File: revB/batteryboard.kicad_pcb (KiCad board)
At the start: 2 copper layers, 90.2 x 101.1 mm, 50 parts, among them J101 KEYSTONE-1042, J102 KEYSTONE-1042, J103 KEYSTONE-1042, J104 KEYSTONE-1042, J105 KEYSTONE-1042, J106 KEYSTONE-1042, J107 Conn_02x10_Top_Bottom, P201 Conn_02x60_Top_Bottom, Q101 IRF7458, Q102 IRF7458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

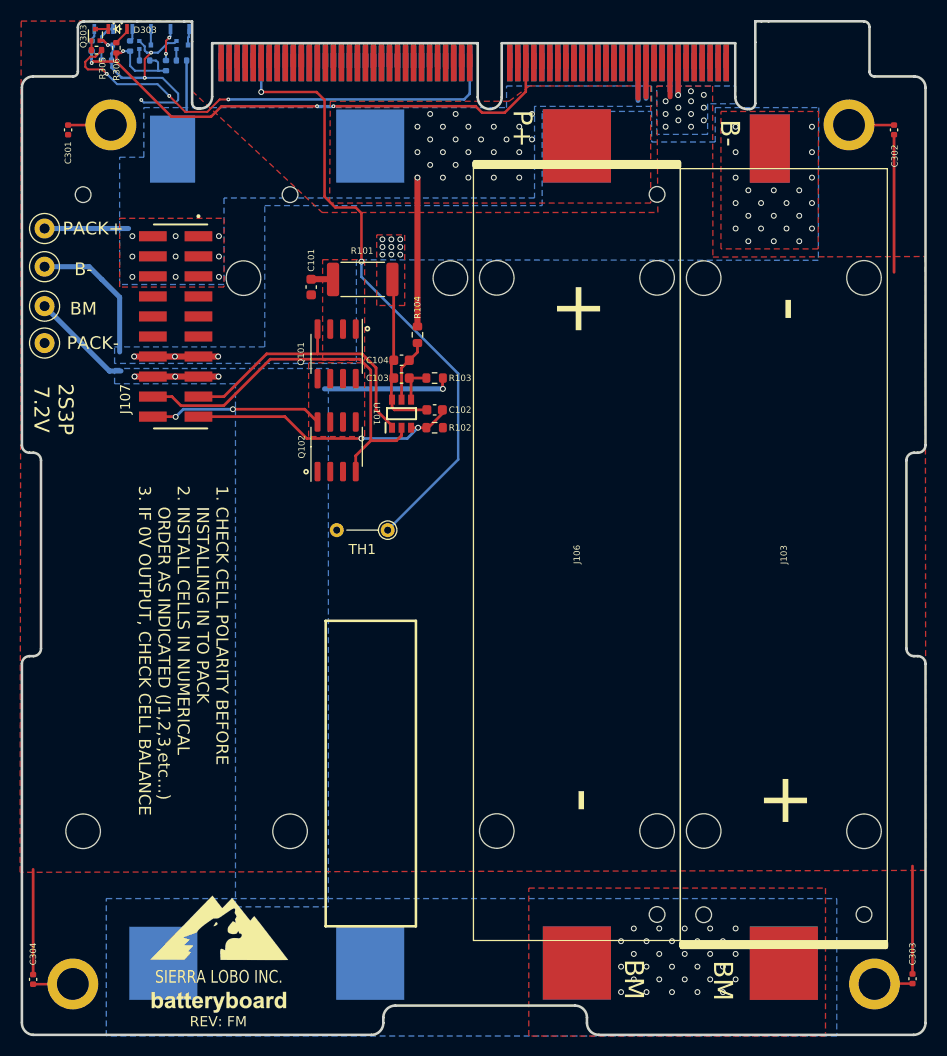
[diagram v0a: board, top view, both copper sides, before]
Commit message: update project to kicad 7 format
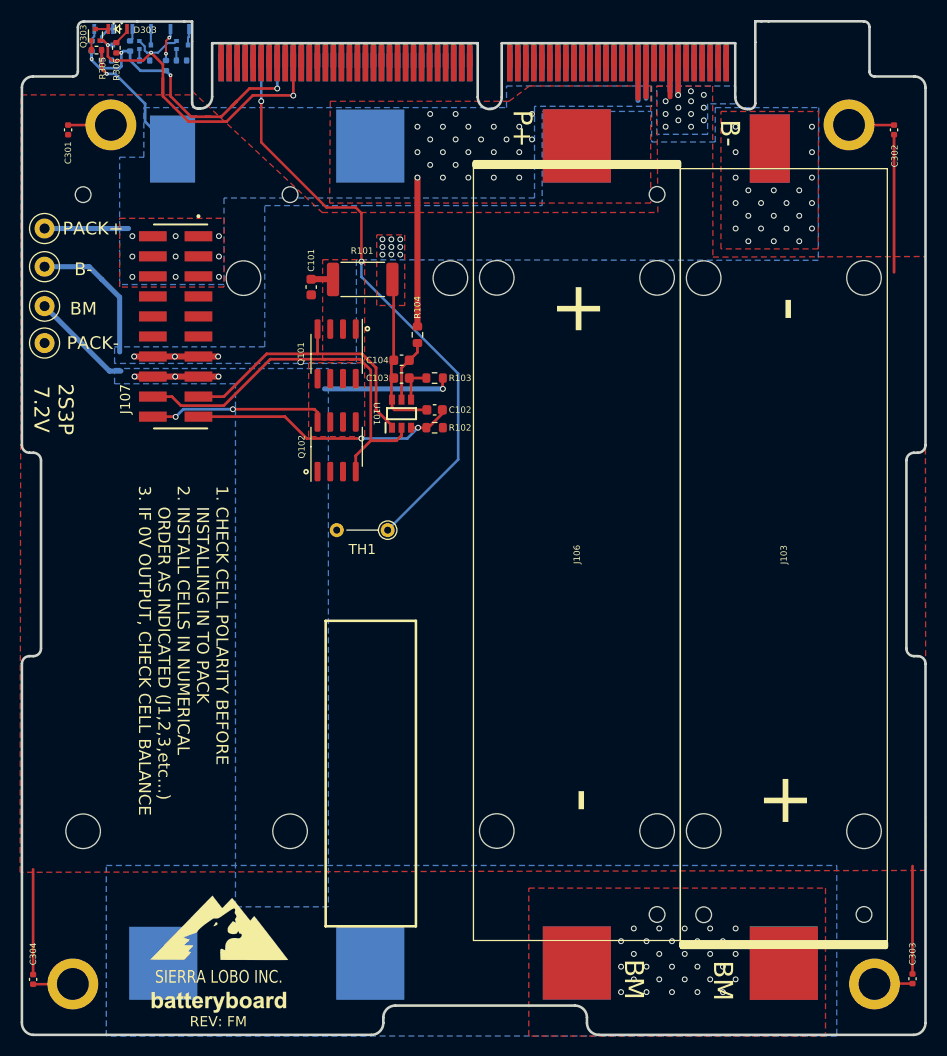
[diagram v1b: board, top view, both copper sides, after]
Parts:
- R301, R303, R305, R307: value 1.5k -> 4.7k
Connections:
- P201 pad 15: /SLI-Card/H2-3 -> /SLI-Card/LED_PWR
- P201 pad 19: /SLI-Card/H2-5 -> /SLI-Card/GND
- P201 pad 20: /SLI-Card/H2-6 -> /SLI-Card/GND
- Q301 pad 3: PACK- -> /SLI-Card/GND
- Q302 pad 2: PACK- -> /SLI-Card/GND
- Q303 pad 2: PACK- -> /SLI-Card/GND
- Q304 pad 2: PACK- -> /SLI-Card/GND
- R301 pad 2: PACK- -> /SLI-Card/Blank-Card-Default/RED_LED
- R302 pad 1: /SLI-Card/5V_USB -> /SLI-Card/LED_PWR
- R303 pad 2: /SLI-Card/5V_USB -> /SLI-Card/Blank-Card-Default/YEL_LED
- R304 pad 1: /SLI-Card/5V_USB -> /SLI-Card/LED_PWR
- R305 pad 2: /SLI-Card/3.3V_SYS -> PACK+
- R306 pad 1: /SLI-Card/5V_USB -> /SLI-Card/LED_PWR
- R307 pad 2: PACK+ -> /SLI-Card/Blank-Card-Default/ORG_LED
- R308 pad 1: /SLI-Card/5V_USB -> /SLI-Card/LED_PWR
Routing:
- net /SLI-Card/5V_USB: track 62.1 -> 0.00 mm, vias 4 -> 0
- net /SLI-Card/3.3V_SYS: track 46.2 -> 0.00 mm, vias 3 -> 0
- net /SLI-Card/GND: track 0.00 -> 36.7 mm, vias 0 -> 3
- net /SLI-Card/LED_PWR: track 0.00 -> 31.5 mm, vias 0 -> 4
- net PACK-: track 69.7 -> 45.9 mm, vias 17 -> 13
- net PACK+: track 40.9 -> 49.1 mm, vias 37 -> 38
- net BAT_THERM: track 61.7 -> 59.0 mm
- net /Q1D_Q2S: track 17.3 -> 17.8 mm
